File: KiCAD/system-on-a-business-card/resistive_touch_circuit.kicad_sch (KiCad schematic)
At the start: 21 parts, among them U5 TCA9535PWR

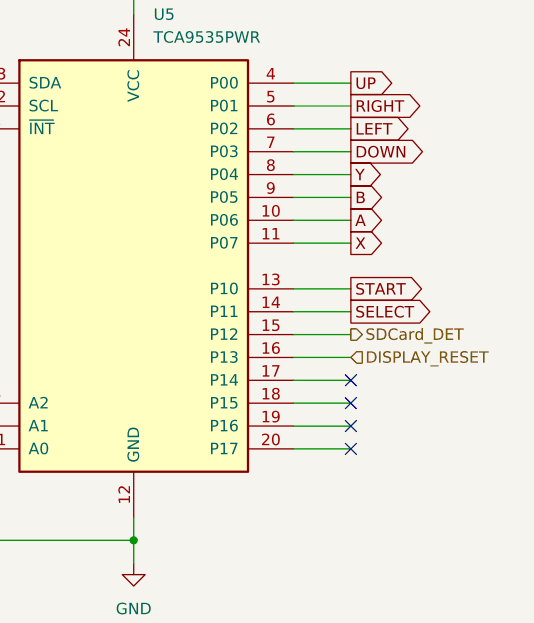
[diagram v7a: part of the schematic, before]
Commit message: #10: created version with DAC, Op Amp and speaker
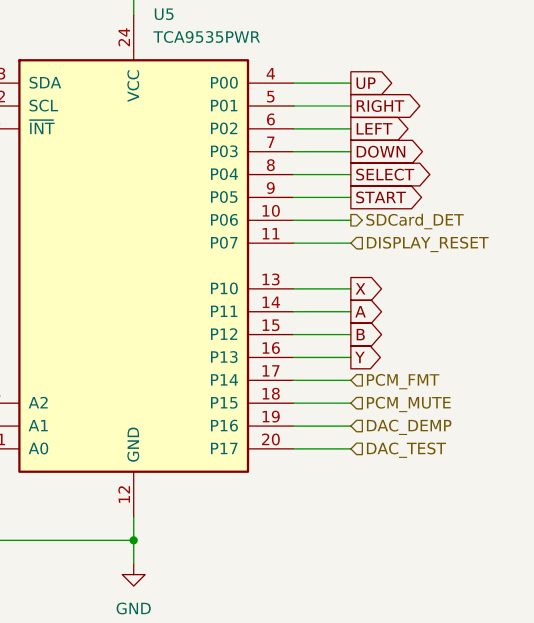
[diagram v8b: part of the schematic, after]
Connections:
- net A: now also U5.14 (P11); no longer U5.10 (P06)
- net B: now also U5.15 (P12); no longer U5.9 (P05)
- net DISPLAY_RESET: now also U5.11 (P07); no longer U5.16 (P13)
- net SDCard_DET: now also U5.10 (P06); no longer U5.15 (P12)
- net SELECT: now also U5.8 (P04); no longer U5.14 (P11)
- net START: now also U5.9 (P05); no longer U5.13 (P10)
- net X: now also U5.13 (P10); no longer U5.11 (P07)
- net Y: now also U5.16 (P13); no longer U5.8 (P04)
- net PCM_FMT: now reaches U5.17 (P14)
- net PCM_MUTE: now reaches U5.18 (P15)
- net DAC_DEMP: now reaches U5.19 (P16)
- net DAC_TEST: now reaches U5.20 (P17)
- no-connect marks 4 -> 0
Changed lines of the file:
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@@
   (junction (at 171.45 96.52) (diameter 0) (color 0 0 0 0)
   )
-  (no_connect (at 195.58 86.36))
-  (no_connect (at 195.58 83.82))
-  (no_connect (at 195.58 78.74))
-  (no_connect (at 195.58 81.28))
   (wire (pts (xy 149.86 83.82) (xy 149.86 86.36))
     (stroke (width 0) (type default))
@@
     (stroke (width 0) (type default))
   )
-  (wire (pts (xy 195.58 86.36) (xy 189.23 86.36))
+  (wire (pts (xy 189.23 86.36) (xy 195.58 86.36))
     (stroke (width 0) (type default))
   )
@@
     )
   )
-  (global_label "X" (shape output) (at 195.58 63.5 0) (fields_autoplaced)
-    (effects (font (size 1.27 1.27)) (justify left))
-    (property "Intersheetrefs" "${INTERSHEET_REFS}" (at 199.7747 63.5 0)
+  (global_label "X" (shape output) (at 195.58 68.58 0) (fields_autoplaced)
+    (effects (font (size 1.27 1.27)) (justify left))
+    (property "Intersheetrefs" "${INTERSHEET_REFS}" (at 199.7747 68.58 0)
       (effects (font (size 1.27 1.27)) (justify left) hide)
     )
@@
     )
   )
-  (global_label "B" (shape output) (at 195.58 58.42 0) (fields_autoplaced)
-    (effects (font (size 1.27 1.27)) (justify left))
-    (property "Intersheetrefs" "${INTERSHEET_REFS}" (at 199.8352 58.42 0)
-      (effects (font (size 1.27 1.27)) (justify left) hide)
-    )
-  )
-  (global_label "SELECT" (shape output) (at 195.58 71.12 0) (fields_autoplaced)
-    (effects (font (size 1.27 1.27)) (justify left))
-    (property "Intersheetrefs" "${INTERSHEET_REFS}" (at 205.3384 71.12 0)
+  (global_label "B" (shape output) (at 195.58 73.66 0) (fields_autoplaced)
+    (effects (font (size 1.27 1.27)) (justify left))
+    (property "Intersheetrefs" "${INTERSHEET_REFS}" (at 199.8352 73.66 0)
+      (effects (font (size 1.27 1.27)) (justify left) hide)
+    )
+  )
+  (global_label "SELECT" (shape output) (at 195.58 55.88 0) (fields_autoplaced)
+    (effects (font (size 1.27 1.27)) (justify left))
+    (property "Intersheetrefs" "${INTERSHEET_REFS}" (at 205.3384 55.88 0)
       (effects (font (size 1.27 1.27)) (justify left) hide)
     )
@@
     )
   )
-  (global_label "Y" (shape output) (at 195.58 55.88 0) (fields_autoplaced)
-    (effects (font (size 1.27 1.27)) (justify left))
-    (property "Intersheetrefs" "${INTERSHEET_REFS}" (at 199.6538 55.88 0)
+  (global_label "Y" (shape output) (at 195.58 76.2 0) (fields_autoplaced)
+    (effects (font (size 1.27 1.27)) (justify left))
+    (property "Intersheetrefs" "${INTERSHEET_REFS}" (at 199.6538 76.2 0)
       (effects (font (size 1.27 1.27)) (justify left) hide)
     )
@@
     )
   )
-  (global_label "A" (shape output) (at 195.58 60.96 0) (fields_autoplaced)
-    (effects (font (size 1.27 1.27)) (justify left))
-    (property "Intersheetrefs" "${INTERSHEET_REFS}" (at 199.6538 60.96 0)
-      (effects (font (size 1.27 1.27)) (justify left) hide)
-    )
-  )
-  (global_label "START" (shape output) (at 195.58 68.58 0) (fields_autoplaced)
-    (effects (font (size 1.27 1.27)) (justify left))
-    (property "Intersheetrefs" "${INTERSHEET_REFS}" (at 204.0685 68.58 0)
+  (global_label "A" (shape output) (at 195.58 71.12 0) (fields_autoplaced)
+    (effects (font (size 1.27 1.27)) (justify left))
+    (property "Intersheetrefs" "${INTERSHEET_REFS}" (at 199.6538 71.12 0)
+      (effects (font (size 1.27 1.27)) (justify left) hide)
+    )
+  )
+  (global_label "START" (shape output) (at 195.58 58.42 0) (fields_autoplaced)
+    (effects (font (size 1.27 1.27)) (justify left))
+    (property "Intersheetrefs" "${INTERSHEET_REFS}" (at 204.0685 58.42 0)
       (effects (font (size 1.27 1.27)) (justify left) hide)
     )
@@
     )
   )
-  (hierarchical_label "DISPLAY_RESET" (shape input) (at 195.58 76.2 0) (fields_autoplaced)
+  (hierarchical_label "DAC_DEMP" (shape input) (at 195.58 83.82 0) (fields_autoplaced)
+    (effects (font (size 1.27 1.27)) (justify left))
+  )
+  (hierarchical_label "DAC_TEST" (shape input) (at 195.58 86.36 0) (fields_autoplaced)
+    (effects (font (size 1.27 1.27)) (justify left))
+  )
+  (hierarchical_label "DISPLAY_RESET" (shape input) (at 195.58 63.5 0) (fields_autoplaced)
     (effects (font (size 1.27 1.27)) (justify left))
   )
@@
     (effects (font (size 1.27 1.27)) (justify right))
   )
+  (hierarchical_label "PCM_MUTE" (shape input) (at 195.58 81.28 0) (fields_autoplaced)
+    (effects (font (size 1.27 1.27)) (justify left))
+  )
+  (hierarchical_label "PCM_FMT" (shape input) (at 195.58 78.74 0) (fields_autoplaced)
+    (effects (font (size 1.27 1.27)) (justify left))
+  )
   (hierarchical_label "INT" (shape input) (at 148.59 50.8 180) (fields_autoplaced)
     (effects (font (size 1.27 1.27)) (justify right))
   )
-  (hierarchical_label "SDCard_DET" (shape output) (at 195.58 73.66 0) (fields_autoplaced)
-    (effects (font (size 1.27 1.27)) (justify left))
-  )
+  (hierarchical_label "SDCard_DET" (shape output) (at 195.58 60.96 0) (fields_autoplaced)
+    (effects (font (size 1.27 1.27)) (justify left))
+  )
